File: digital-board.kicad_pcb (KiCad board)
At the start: 2 copper layers, 200 x 140 mm, 193 parts, among them IC1 ATMEGA6450-A, J1 CONN_20X2, Q1 2N3904, Q10 2N3904, Q11 2N3904, Q12 2N3904, Q13 2N3904, Q14 2N3904, Q15 2N3904, Q2 2N3904, Q3 2N3904, Q4 2N3904, Q5 2N3904, Q6 2N3904, Q7 2N3904, Q8 2N3904, Q9 2N3904, SW15 TACT_SWITCH, SW16 TACT_SWITCH, SW17 TACT_SWITCH, SW18 TACT_SWITCH, SW19 TACT_SWITCH, SW20 TACT_SWITCH, SW21 TACT_SWITCH, SW22 TACT_SWITCH, U1 DG419, U2 74HC4067, U3 R-78E5.0-1.0, U4 74HC4067, U5 74LS573, U6 74LS573, U7 74LVC2G04, U8 74LS573, U9 74LS573, X1 MIDI OUT, X2 MIDI IN, X3 MIDI THRU

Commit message: commit
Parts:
- moved VR19 196.1 mm to (191.0, 58.0)
- moved VR15 188.6 mm to (191.0, 37.0)
- moved VR12 183.7 mm to (191.0, 18.0)
- moved VR18 182.5 mm to (176.0, 58.0)
- moved VR14 174.4 mm to (176.0, 37.0)
- moved VR17 169.1 mm to (161.0, 58.0)
- moved VR13 160.4 mm to (161.0, 37.0)
- moved VR16 156.0 mm to (146.0, 58.0)
- moved VR11 154.5 mm to (161.0, 18.0)
- moved ISW9 146.9 mm to (146.0, 38.0)
- moved VR10 140.0 mm to (146.0, 18.0)
- moved VR7 128.8 mm to (126.0, 38.0)
- moved ISW8 127.0 mm to (111.0, 58.0)
- moved VR4 121.0 mm to (126.0, 18.0)
- moved LED16 119.9 mm to (40.0, 95.5)
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
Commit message: commit
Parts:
- moved VR31 221.9 mm to (176.0, 128.0)
- moved VR28 221.0 mm to (191.0, 108.0)
- moved VR30 211.1 mm to (161.0, 128.0)
- moved VR27 209.0 mm to (176.0, 108.0)
- moved VR24 205.0 mm to (191.0, 78.0)
- moved VR29 200.7 mm to (146.0, 128.0)
- moved VR26 197.5 mm to (161.0, 108.0)
- moved VR23 192.0 mm to (176.0, 78.0)
- moved VR25 186.4 mm to (146.0, 108.0)
- moved VR22 179.3 mm to (161.0, 78.0)
- moved LED30 161.7 mm to (85.0, 123.0)
- moved SW22 158.2 mm to (111.0, 102.0)
- moved ISW14 158.1 mm to (126.0, 88.0)
- moved LED29 157.2 mm to (85.0, 118.0)
- moved LED27 153.6 mm to (65.0, 123.0)
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
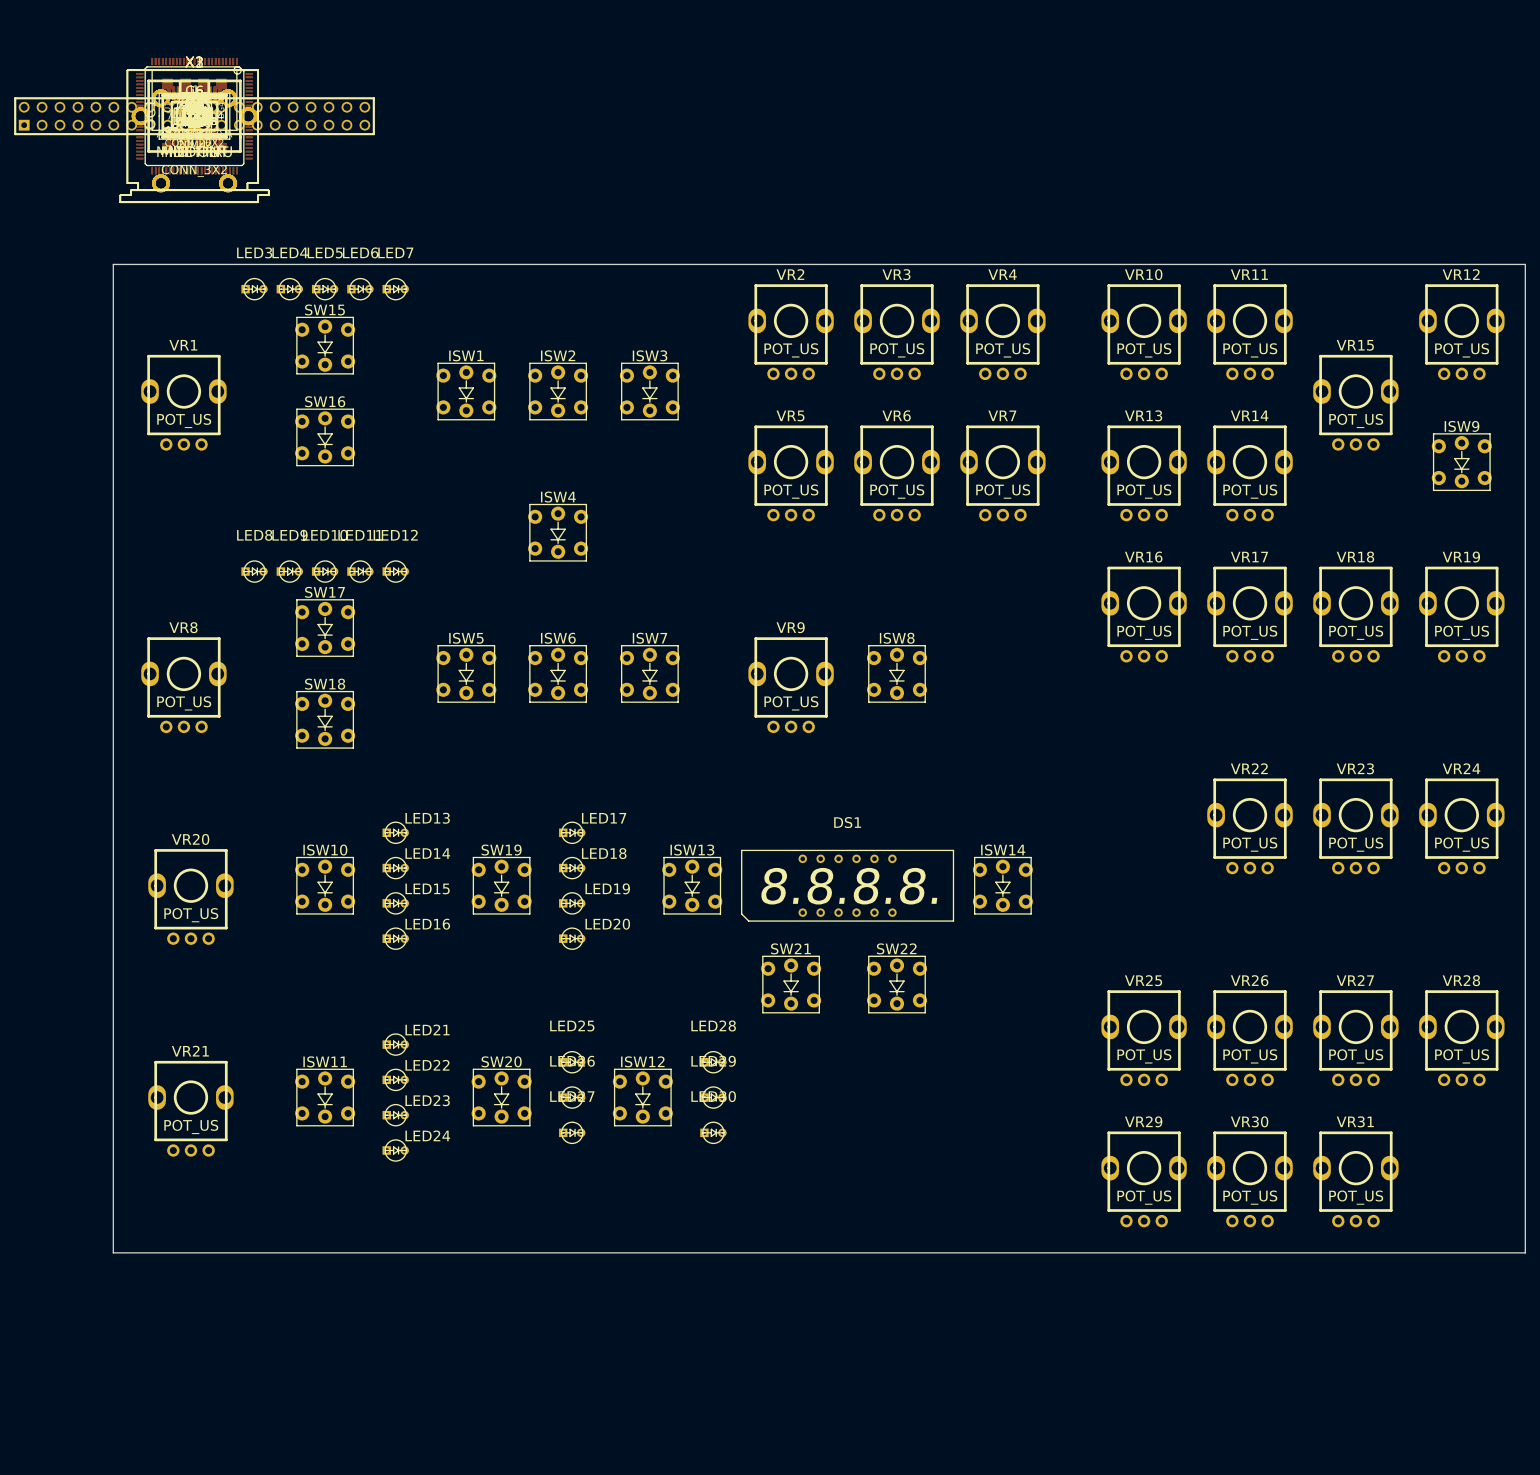
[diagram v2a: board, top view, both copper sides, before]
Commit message: finished pot/switch layout
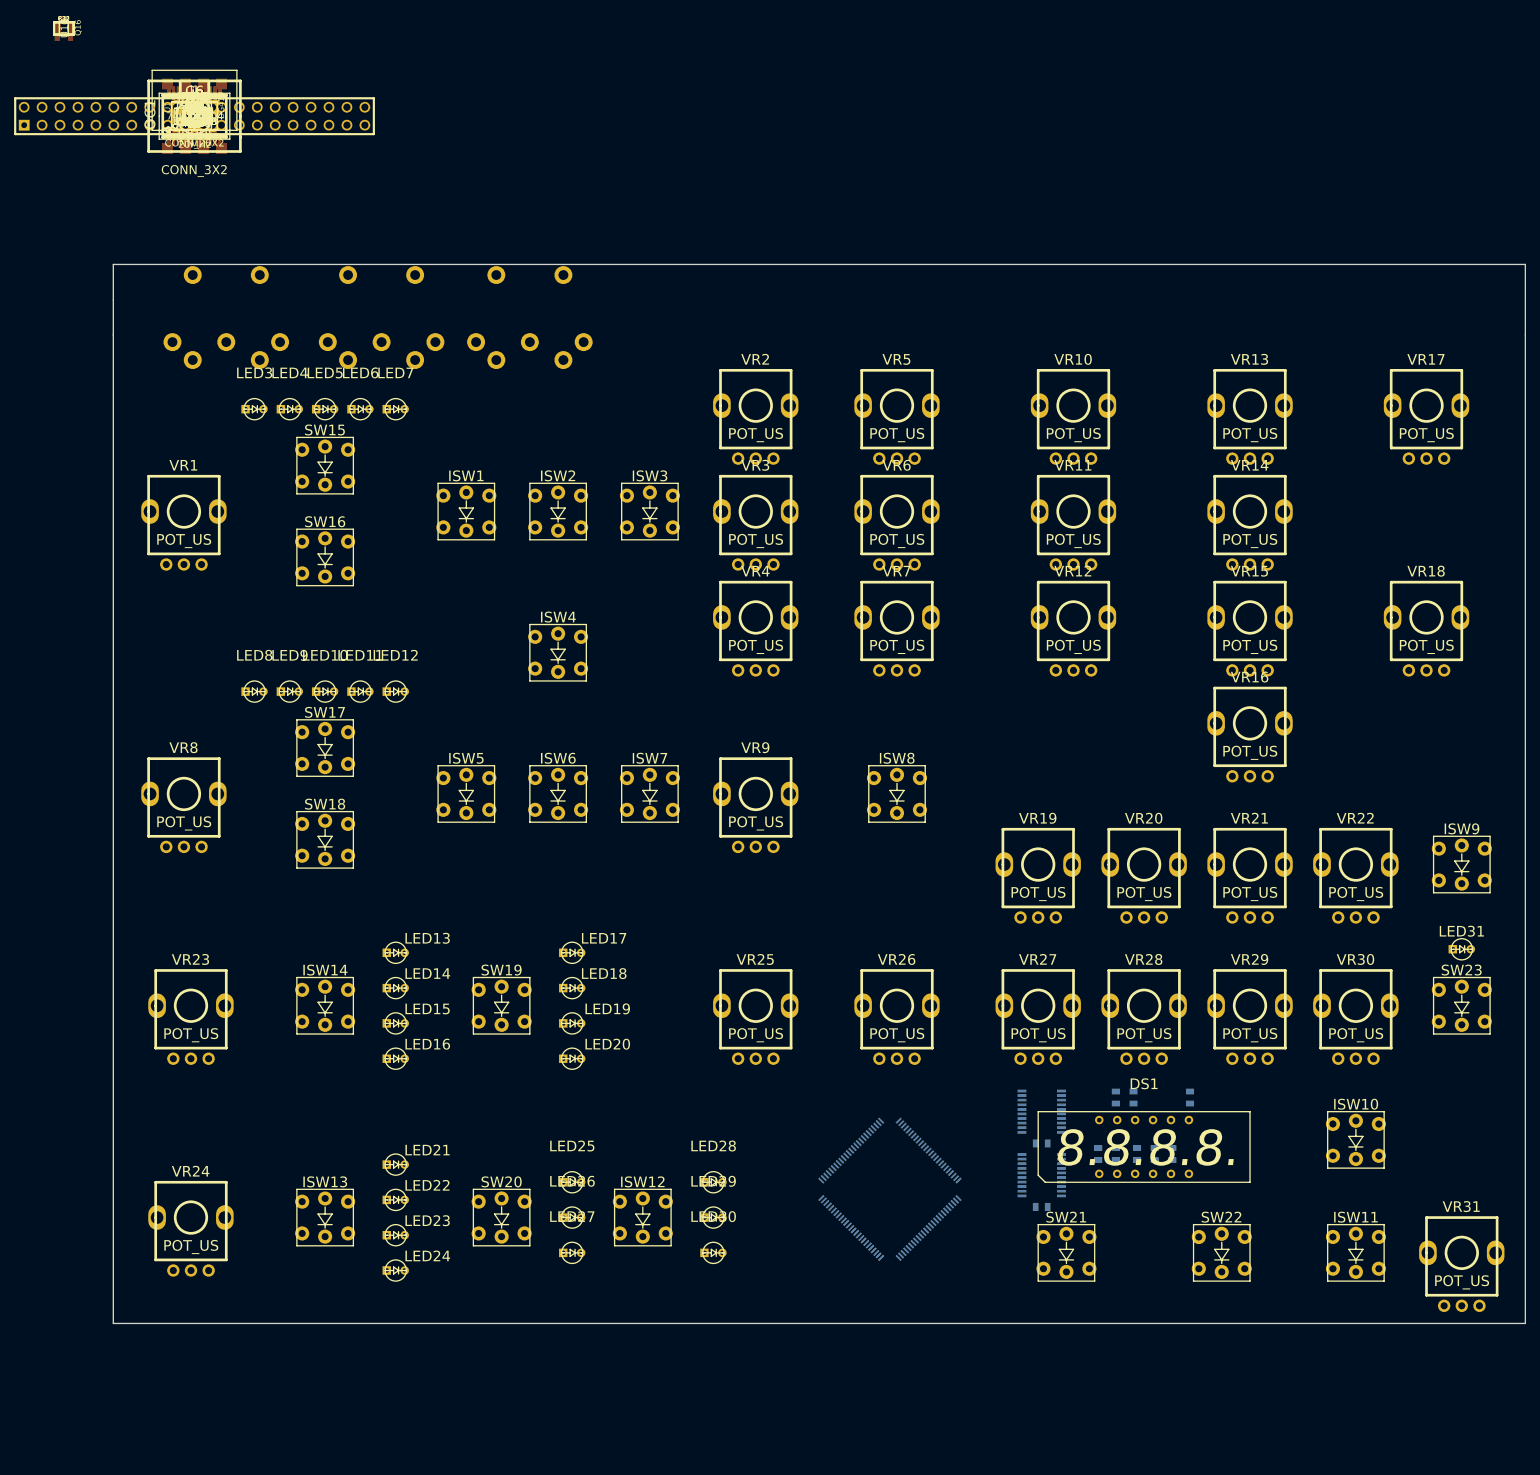
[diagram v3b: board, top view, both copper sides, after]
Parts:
- added C17: 0.1µ, synth:SM0603-JRL, F.Cu at (-7.00, -33.4)
- added LED31: LED, MyModules:3MM-LED, F.Cu at (191.0, 97.0)
- added Q16: 2N3904, synth:SOT23-JRL, F.Cu at (-7.00, -33.4)
- added R30: 10K, synth:SM0603-JRL, F.Cu at (-7.00, -33.4)
- added R31: 330, synth:SM0603-JRL, F.Cu at (-7.00, -33.4)
- added SW23: TACT_SWITCH, MyModules:TL1240, F.Cu at (191.0, 105.0)
- added U10: 74LVC1G32, github-smd:SOT-353, F.Cu at (-7.00, -33.4)
- C10, C11, IC1, R10, R11, R12, R14, R15, R16, R17, R9, U5, U6, X1, X2, X3: moved to B.Cu
- moved R16 202.0 mm to (150.0, 126.0), turned to 90 degrees
- moved R11 200.3 mm to (147.5, 126.0), turned to 90 degrees
- moved R17 198.6 mm to (145.0, 126.0), turned to 90 degrees
- moved R10 198.0 mm to (152.5, 118.0), turned to 90 degrees
- moved R12 196.6 mm to (142.0, 126.0), turned to 90 degrees
- moved C11 195.6 mm to (131.5, 133.5), turned to 180 degrees
- moved R14 194.9 mm to (139.5, 126.0), turned to 90 degrees
- moved R15 192.4 mm to (144.5, 118.0), turned to 90 degrees
- moved U5 192.1 mm to (131.5, 129.0), turned to 90 degrees
- moved R9 190.7 mm to (142.0, 118.0), turned to 90 degrees
- moved VR24 188.8 mm to (11.0, 135.0)
- moved C10 188.6 mm to (131.5, 124.5), turned to 180 degrees
- moved U6 185.1 mm to (131.5, 120.0), turned to 90 degrees
- moved IC1 181.1 mm to (110.0, 131.0), turned to 315 degrees
- moved VR23 167.2 mm to (11.0, 105.0)
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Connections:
- IC1 pad 93: GATE -> DGATE
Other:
- board size 200 x 140 mm -> 200 x 150 mm

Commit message: last commit before branch
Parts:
- C1, C14, C16, C2, C3, C5, D1, D2, ISP1, L1, LED1, OC1, Q10, Q11, Q12, Q13, Q14, Q15, R1, R13, R18, R19, R2, R4, R7, R8, TP2, TP8, U1, U7, U9, XTAL1: moved to B.Cu
- moved C1 193.8 mm to (114.0, 143.5), turned to 180 degrees
- moved C5 193.5 mm to (110.0, 145.5), turned to 180 degrees
- moved L1 191.7 mm to (110.0, 143.5)
- moved LED1 191.4 mm to (106.0, 145.5)
- moved R4 189.7 mm to (106.0, 143.5)
- moved ISP1 185.6 mm to (95.5, 144.5)
- moved U1 177.7 mm to (121.0, 119.0), turned to 270 degrees
- moved TP2 176.1 mm to (96.0, 133.5)
- moved R2 173.0 mm to (96.0, 130.0), turned to 180 degrees
- moved R1 170.9 mm to (96.0, 127.5)
- moved XTAL1 169.7 mm to (100.5, 123.5), turned to 225 degrees
- moved C2 167.0 mm to (96.0, 123.0)
- moved Q10 166.9 mm to (147.0, 76.5), turned to 90 degrees
- moved C3 164.8 mm to (96.0, 120.5)
- moved Q11 164.6 mm to (147.0, 72.5), turned to 90 degrees
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
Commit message: laying out board with led rework changes
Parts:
- removed D10, D11, D12, D13, D14, D15, D16, D17, D18, D19, D2, D20, D21, D22, D23, D3, D4, D5, D6, D7, D8, D9: 1N4148, synth:SOD323-JRL
- removed Q10, Q11, Q12, Q13, Q14, Q15, Q16, Q3, Q4, Q5, Q6, Q7, Q8, Q9: 2N3904, synth:SOT23-JRL
- added C18, C19, C20, C21, C22: 0.1µ, synth:SM0603-JRL, F.Cu at (100.0, 160.1)
- added R32, R33, R35, R38, R39, R42, R43, R49, R52, R54, R57, R58, R61, R62, R64, R66, R67, R69, R70, R72, R73, R75, R76, R78, R80, R81, R83, R84, R86, R87, R89, R90, R91: 470, synth:SM0603-JRL, F.Cu at (100.0, 160.1)
- added R34, R36, R37, R40, R41, R44, R45, R50, R51, R53, R55, R56, R59, R60, R63, R65, R68, R71, R74, R77, R79, R82, R85, R88, R92: 10K, synth:SM0603-JRL, F.Cu at (100.0, 160.1)
- added R46, R47, R48: 1K, synth:SM0603-JRL, F.Cu at (100.0, 160.1)
- added TP10, TP11, TP12, TP13, TP9: CONN_1, MyModules:TEST POINT, F.Cu at (100.0, 160.1)
- added U11: 74HC165, github-smd:TSSOP-16, F.Cu at (51.2, 166.0)
- added U12: 74AC595, github-smd:TSSOP-16, F.Cu at (85.0, 164.5)
- added U13: 74AC595, github-smd:TSSOP-16, F.Cu at (69.5, 165.0)
- added U14: 74HC165, github-smd:TSSOP-16, F.Cu at (45.2, 158.2)
- added U15: 74AC595, github-smd:TSSOP-16, F.Cu at (62.2, 163.5)
- added U16: 74AC595, github-smd:TSSOP-16, F.Cu at (78.5, 165.0)
- TP2: moved to F.Cu
- U8: value 74LS573 -> 74AC595; footprint MyModules:TSSOP-20 -> github-smd:TSSOP-16
- U9: value 74LS573 -> 74HC165; footprint MyModules:TSSOP-20 -> github-smd:TSSOP-16
- moved TP7 220.0 mm to (134.6, 161.3)
- moved TP6 217.9 mm to (130.8, 161.3)
- moved TP5 215.8 mm to (127.0, 161.3)
- moved TP4 213.8 mm to (123.2, 161.3)
- moved TP3 211.8 mm to (119.4, 161.3)
- moved TP1 208.0 mm to (111.8, 161.3)
- moved TP8 60.3 mm to (138.4, 161.3)
- moved TP2 34.0 mm to (115.6, 161.3)
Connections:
- IC1 pad 19: ANALOG SW LATCH -> ~SPI_EN
- IC1 pad 24: SW ROW 0 -> SWITCH_LATCH
- IC1 pad 25: SW ROW 1 -> LED_LATCH
- IC1 pad 26: SW ROW 3 -> ARP_SYNC
- IC1 pad 43: DAC MUX EN0 -> Net-(IC1-Pad43)
- IC1 pad 44: DAC MUX EN1 -> Net-(IC1-Pad44)
- IC1 pad 45: DAC MUX EN2 -> Net-(IC1-Pad45)
- IC1 pad 46: DAC MUX EN3 -> Net-(IC1-Pad46)
- IC1 pad 47: DISP CATHODE LATCH -> Net-(IC1-Pad47)
- IC1 pad 48: DISP ANODE LATCH -> Net-(IC1-Pad48)
- IC1 pad 49: LED ANODE LATCH -> Net-(IC1-Pad49)
- IC1 pad 50: LED CATHODE LATCH -> Net-(IC1-Pad50)
- IC1 pad 53: SW COL 0 -> DAC MUX EN0
- IC1 pad 54: SW COL 1 -> DAC MUX EN1
- IC1 pad 55: SW COL 2 -> DAC MUX EN2
- IC1 pad 56: SW COL 3 -> DAC MUX EN3
- IC1 pad 57: SW COL 4 -> DISP CATHODE LATCH
- IC1 pad 58: SW COL 5 -> DISP ANODE LATCH
- IC1 pad 68: SW COL 6 -> ANALOG SW LATCH
- IC1 pad 69: SW COL 7 -> Net-(IC1-Pad69)
- ISW1 pad 1: Net-(D2-Pad1) -> +5V
- ISW1 pad 2: Net-(D2-Pad1) -> +5V
- ISW1 pad 3: SW ROW 0 -> Net-(ISW1-Pad3)
- ISW1 pad 4: SW ROW 0 -> Net-(ISW1-Pad3)
- ISW1 pad 5: Net-(ISW1-Pad5) -> GND
- ISW10 pad 1: Net-(D6-Pad1) -> +5V
- ISW10 pad 2: Net-(D6-Pad1) -> +5V
- ISW10 pad 3: SW ROW 1 -> Net-(ISW10-Pad3)
- ISW10 pad 4: SW ROW 1 -> Net-(ISW10-Pad3)
- ISW10 pad 5: Net-(ISW10-Pad5) -> GND
- ISW11 pad 1: Net-(D9-Pad1) -> +5V
- ISW11 pad 2: Net-(D9-Pad1) -> +5V
- ISW11 pad 3: SW ROW 1 -> Net-(ISW11-Pad3)
- ISW11 pad 4: SW ROW 1 -> Net-(ISW11-Pad3)
- ISW11 pad 5: Net-(ISW11-Pad5) -> GND
- ISW11 pad 6: Net-(ISW10-Pad6) -> Net-(ISW11-Pad6)
- ISW12 pad 1: Net-(D12-Pad1) -> +5V
- ISW12 pad 2: Net-(D12-Pad1) -> +5V
- ISW12 pad 3: SW ROW 1 -> Net-(ISW12-Pad3)
- ISW12 pad 4: SW ROW 1 -> Net-(ISW12-Pad3)
- ISW12 pad 5: Net-(ISW1-Pad5) -> GND
- ISW13 pad 1: Net-(D15-Pad1) -> +5V
- ISW13 pad 2: Net-(D15-Pad1) -> +5V
- ISW13 pad 3: SW ROW 1 -> Net-(ISW13-Pad3)
- ISW13 pad 4: SW ROW 1 -> Net-(ISW13-Pad3)
- ISW13 pad 5: Net-(ISW13-Pad5) -> GND
- ISW14 pad 1: Net-(D18-Pad1) -> +5V
- ISW14 pad 2: Net-(D18-Pad1) -> +5V
- ISW14 pad 3: SW ROW 1 -> Net-(ISW14-Pad3)
- ISW14 pad 4: SW ROW 1 -> Net-(ISW14-Pad3)
- ISW2 pad 1: Net-(D5-Pad1) -> +5V
- ISW2 pad 2: Net-(D5-Pad1) -> +5V
- ISW2 pad 3: SW ROW 0 -> Net-(ISW2-Pad3)
- ISW2 pad 4: SW ROW 0 -> Net-(ISW2-Pad3)
- ISW2 pad 5: Net-(ISW13-Pad5) -> GND
- ISW2 pad 6: Net-(ISW1-Pad6) -> Net-(ISW2-Pad6)
- ISW3 pad 1: Net-(D8-Pad1) -> +5V
- ISW3 pad 2: Net-(D8-Pad1) -> +5V
- ISW3 pad 3: SW ROW 0 -> Net-(ISW3-Pad3)
- ISW3 pad 4: SW ROW 0 -> Net-(ISW3-Pad3)
- ISW3 pad 5: Net-(ISW3-Pad5) -> GND
- ISW3 pad 6: Net-(ISW1-Pad6) -> Net-(ISW3-Pad6)
- ISW4 pad 1: Net-(D11-Pad1) -> +5V
- ISW4 pad 2: Net-(D11-Pad1) -> +5V
- ISW4 pad 3: SW ROW 0 -> Net-(ISW4-Pad3)
- ISW4 pad 4: SW ROW 0 -> Net-(ISW4-Pad3)
- ISW4 pad 5: Net-(ISW10-Pad5) -> GND
- ISW4 pad 6: Net-(ISW1-Pad6) -> Net-(ISW4-Pad6)
- ISW5 pad 1: Net-(D14-Pad1) -> +5V
- ISW5 pad 2: Net-(D14-Pad1) -> +5V
- ISW5 pad 3: SW ROW 0 -> Net-(ISW5-Pad3)
- ISW5 pad 4: SW ROW 0 -> Net-(ISW5-Pad3)
- ISW5 pad 5: Net-(ISW11-Pad5) -> GND
- ISW5 pad 6: Net-(ISW1-Pad6) -> Net-(ISW5-Pad6)
- ISW6 pad 1: Net-(D17-Pad1) -> +5V
- ISW6 pad 2: Net-(D17-Pad1) -> +5V
- ISW6 pad 3: SW ROW 0 -> Net-(ISW6-Pad3)
- ISW6 pad 4: SW ROW 0 -> Net-(ISW6-Pad3)
- ISW6 pad 5: Net-(ISW6-Pad5) -> GND
- ISW6 pad 6: Net-(ISW1-Pad6) -> Net-(ISW6-Pad6)
- ISW7 pad 1: Net-(D20-Pad1) -> +5V
- ISW7 pad 2: Net-(D20-Pad1) -> +5V
- ISW7 pad 3: SW ROW 0 -> Net-(ISW7-Pad3)
- ISW7 pad 4: SW ROW 0 -> Net-(ISW7-Pad3)
- ISW7 pad 5: Net-(ISW1-Pad5) -> GND
- ISW7 pad 6: Net-(ISW10-Pad6) -> Net-(ISW7-Pad6)
- ISW8 pad 1: Net-(D22-Pad1) -> +5V
- ISW8 pad 2: Net-(D22-Pad1) -> +5V
- ISW8 pad 3: SW ROW 0 -> Net-(ISW8-Pad3)
- ISW8 pad 4: SW ROW 0 -> Net-(ISW8-Pad3)
- ISW8 pad 5: Net-(ISW13-Pad5) -> GND
- ISW8 pad 6: Net-(ISW10-Pad6) -> Net-(ISW8-Pad6)
- ISW9 pad 1: Net-(D3-Pad1) -> +5V
- ISW9 pad 2: Net-(D3-Pad1) -> +5V
- ISW9 pad 3: SW ROW 1 -> Net-(ISW9-Pad3)
- ISW9 pad 4: SW ROW 1 -> Net-(ISW9-Pad3)
- ISW9 pad 5: Net-(ISW3-Pad5) -> GND
- ISW9 pad 6: Net-(ISW10-Pad6) -> Net-(ISW9-Pad6)
- LED10 pad 2: Net-(ISW11-Pad5) -> GND
- LED11 pad 2: Net-(ISW1-Pad5) -> GND
- LED12 pad 2: Net-(ISW13-Pad5) -> GND
- LED13 pad 1: Net-(LED12-Pad1) -> Net-(LED13-Pad1)
- LED13 pad 2: Net-(ISW3-Pad5) -> GND
- LED14 pad 1: Net-(LED12-Pad1) -> Net-(LED14-Pad1)
- LED14 pad 2: Net-(ISW10-Pad5) -> GND
- LED15 pad 1: Net-(LED12-Pad1) -> Net-(LED15-Pad1)
- LED15 pad 2: Net-(ISW11-Pad5) -> GND
- LED16 pad 2: Net-(ISW1-Pad5) -> GND
- LED17 pad 2: Net-(ISW13-Pad5) -> GND
- LED18 pad 1: Net-(LED17-Pad1) -> Net-(LED18-Pad1)
- LED18 pad 2: Net-(ISW3-Pad5) -> GND
- LED19 pad 1: Net-(LED17-Pad1) -> Net-(LED19-Pad1)
- LED19 pad 2: Net-(ISW10-Pad5) -> GND
- LED20 pad 1: Net-(LED17-Pad1) -> Net-(LED20-Pad1)
- LED20 pad 2: Net-(ISW11-Pad5) -> GND
- LED21 pad 2: Net-(ISW1-Pad5) -> GND
- LED22 pad 2: Net-(ISW13-Pad5) -> GND
- LED23 pad 1: Net-(LED22-Pad1) -> Net-(LED23-Pad1)
- LED23 pad 2: Net-(ISW3-Pad5) -> GND
- LED24 pad 1: Net-(LED22-Pad1) -> Net-(LED24-Pad1)
- LED24 pad 2: Net-(ISW10-Pad5) -> GND
- LED25 pad 1: Net-(LED22-Pad1) -> Net-(LED25-Pad1)
- LED25 pad 2: Net-(ISW11-Pad5) -> GND
- LED26 pad 2: Net-(ISW1-Pad5) -> GND
- LED27 pad 2: Net-(ISW13-Pad5) -> GND
- LED28 pad 1: Net-(LED27-Pad1) -> Net-(LED28-Pad1)
- LED28 pad 2: Net-(ISW3-Pad5) -> GND
- LED29 pad 1: Net-(LED27-Pad1) -> Net-(LED29-Pad1)
- LED29 pad 2: Net-(ISW10-Pad5) -> GND
- LED3 pad 1: Net-(ISW13-Pad6) -> Net-(LED3-Pad1)
- LED3 pad 2: Net-(ISW3-Pad5) -> GND
- LED30 pad 1: Net-(LED27-Pad1) -> Net-(LED30-Pad1)
- LED30 pad 2: Net-(ISW11-Pad5) -> GND
- LED4 pad 1: Net-(ISW13-Pad6) -> Net-(LED4-Pad1)
- LED4 pad 2: Net-(ISW10-Pad5) -> GND
- LED5 pad 1: Net-(ISW13-Pad6) -> Net-(LED5-Pad1)
- LED5 pad 2: Net-(ISW11-Pad5) -> GND
- LED6 pad 2: Net-(ISW1-Pad5) -> GND
- LED7 pad 1: Net-(LED10-Pad1) -> Net-(LED7-Pad1)
- LED7 pad 2: Net-(ISW13-Pad5) -> GND
- LED8 pad 1: Net-(LED10-Pad1) -> Net-(LED8-Pad1)
- LED8 pad 2: Net-(ISW3-Pad5) -> GND
- LED9 pad 1: Net-(LED10-Pad1) -> Net-(LED9-Pad1)
- LED9 pad 2: Net-(ISW10-Pad5) -> GND
- R22 pad 2: Net-(Q2-Pad1) -> Net-(R22-Pad2)
- R23 pad 1: Net-(ISW10-Pad6) -> Net-(ISW2-Pad6)
- R24 pad 1: Net-(ISW12-Pad6) -> Net-(ISW3-Pad6)
- R25 pad 1: Net-(LED6-Pad1) -> Net-(ISW4-Pad6)
- R26 pad 1: Net-(LED11-Pad1) -> Net-(ISW5-Pad6)
- R27 pad 1: Net-(LED16-Pad1) -> Net-(ISW6-Pad6)
- R28 pad 1: Net-(LED21-Pad1) -> Net-(ISW7-Pad6)
- R29 pad 1: Net-(LED26-Pad1) -> Net-(ISW8-Pad6)
- R30 pad 1: Net-(Q16-Pad2) -> Net-(Q2-Pad2)
- R31 pad 1: Net-(Q16-Pad1) -> Net-(Q2-Pad1)
- SW15 pad 1: Net-(D21-Pad1) -> +5V
- SW15 pad 2: Net-(D21-Pad1) -> +5V
- SW15 pad 3: SW ROW 1 -> Net-(R88-Pad2)
- SW15 pad 4: SW ROW 1 -> Net-(R88-Pad2)
- SW16 pad 1: Net-(D23-Pad1) -> +5V
- SW16 pad 2: Net-(D23-Pad1) -> +5V
- SW16 pad 3: SW ROW 1 -> Net-(R36-Pad2)
- SW16 pad 4: SW ROW 1 -> Net-(R36-Pad2)
- SW17 pad 1: Net-(D4-Pad1) -> +5V
- SW17 pad 2: Net-(D4-Pad1) -> +5V
- SW17 pad 3: SW ROW 2 -> Net-(R40-Pad2)
- SW17 pad 4: SW ROW 2 -> Net-(R40-Pad2)
- SW18 pad 1: Net-(D7-Pad1) -> +5V
- SW18 pad 2: Net-(D7-Pad1) -> +5V
- SW18 pad 3: SW ROW 2 -> Net-(R44-Pad2)
- SW18 pad 4: SW ROW 2 -> Net-(R44-Pad2)
- SW19 pad 1: Net-(D10-Pad1) -> +5V
- SW19 pad 2: Net-(D10-Pad1) -> +5V
- SW19 pad 3: SW ROW 2 -> Net-(R50-Pad2)
- SW19 pad 4: SW ROW 2 -> Net-(R50-Pad2)
- SW20 pad 1: Net-(D13-Pad1) -> +5V
- SW20 pad 2: Net-(D13-Pad1) -> +5V
- SW20 pad 3: SW ROW 2 -> Net-(R63-Pad2)
- SW20 pad 4: SW ROW 2 -> Net-(R63-Pad2)
- SW21 pad 1: Net-(D16-Pad1) -> +5V
- SW21 pad 2: Net-(D16-Pad1) -> +5V
- SW21 pad 3: SW ROW 2 -> Net-(R56-Pad2)
- SW21 pad 4: SW ROW 2 -> Net-(R56-Pad2)
- SW22 pad 1: Net-(D19-Pad1) -> +5V
- SW22 pad 2: Net-(D19-Pad1) -> +5V
- SW22 pad 3: SW ROW 2 -> Net-(R60-Pad2)
- SW22 pad 4: SW ROW 2 -> Net-(R60-Pad2)
- TP1 pad 1: FREQ IN -> Net-(IC1-Pad43)
- TP2 pad 1: Net-(IC1-Pad28) -> Net-(IC1-Pad44)
- TP3 pad 1: Net-(IC1-Pad5) -> Net-(IC1-Pad45)
- TP4 pad 1: Net-(IC1-Pad6) -> Net-(IC1-Pad46)
- TP5 pad 1: Net-(IC1-Pad7) -> Net-(IC1-Pad47)
- TP6 pad 1: Net-(IC1-Pad8) -> Net-(IC1-Pad48)
- TP7 pad 1: Net-(IC1-Pad9) -> Net-(IC1-Pad49)
- TP8 pad 1: Net-(C3-Pad2) -> Net-(IC1-Pad50)
- U8 pad 1: GND -> Net-(R33-Pad2)
- U8 pad 10: GND -> +5V
- U8 pad 11: LED ANODE LATCH -> SPI_SCK
- U8 pad 12: Net-(Q9-Pad2) -> LED_LATCH
- U8 pad 13: Net-(Q8-Pad2) -> ~SPI_EN
- U8 pad 14: Net-(Q7-Pad2) -> SPI_MOSI
- U8 pad 16: Net-(Q5-Pad2) -> +5V
- U8 pad 2: DB0 -> Net-(R35-Pad2)
- U8 pad 3: DB1 -> Net-(R38-Pad2)
- U8 pad 4: DB2 -> Net-(R39-Pad2)
- U8 pad 5: DB3 -> Net-(R42-Pad2)
- U8 pad 6: DB4 -> Net-(R43-Pad2)
- U8 pad 7: DB5 -> Net-(R49-Pad2)
- U8 pad 8: DB6 -> GND
- U8 pad 9: DB7 -> Net-(U12-Pad14)
- U9 pad 1: GND -> SWITCH_LATCH
- U9 pad 10: GND -> Net-(U9-Pad10)
- U9 pad 11: LED CATHODE LATCH -> Net-(R36-Pad2)
- U9 pad 12: Net-(U9-Pad12) -> Net-(R40-Pad2)
- U9 pad 13: Net-(U9-Pad13) -> Net-(R44-Pad2)
- U9 pad 14: Net-(Q15-Pad2) -> Net-(R50-Pad2)
- U9 pad 15: Net-(Q14-Pad2) -> GND
- U9 pad 16: Net-(Q13-Pad2) -> +5V
- U9 pad 2: DB0 -> SPI_SCK
- U9 pad 3: DB1 -> Net-(ISW14-Pad3)
- U9 pad 4: DB2 -> Net-(ISW13-Pad3)
- U9 pad 5: DB3 -> Net-(R63-Pad2)
- U9 pad 6: DB4 -> Net-(ISW12-Pad3)
- U9 pad 7: DB5 -> Net-(U9-Pad7)
- U9 pad 8: DB6 -> GND
- U9 pad 9: DB7 -> Net-(U14-Pad10)
